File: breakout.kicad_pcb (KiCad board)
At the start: 2 copper layers, 50 x 50 mm, 98 parts

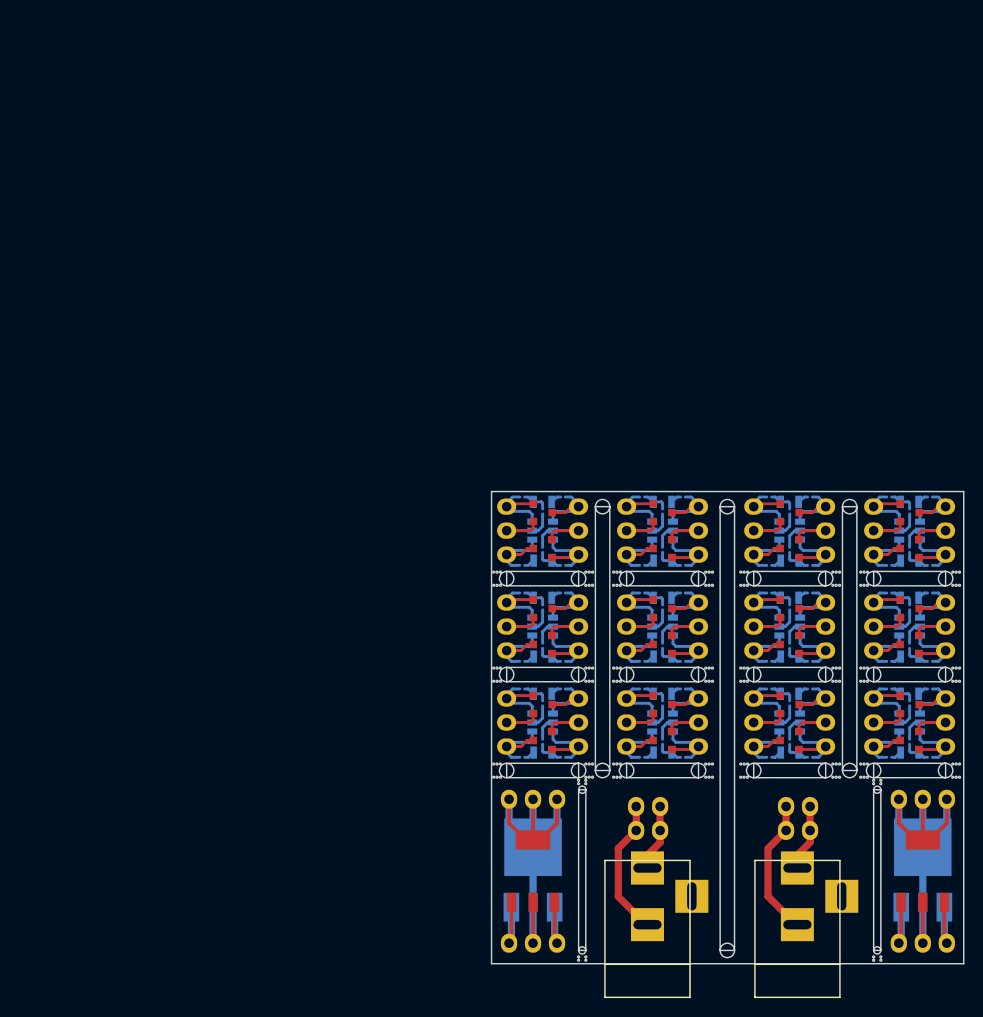
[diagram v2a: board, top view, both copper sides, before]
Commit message: 10x10 breakout with soic-8 and tssop-8
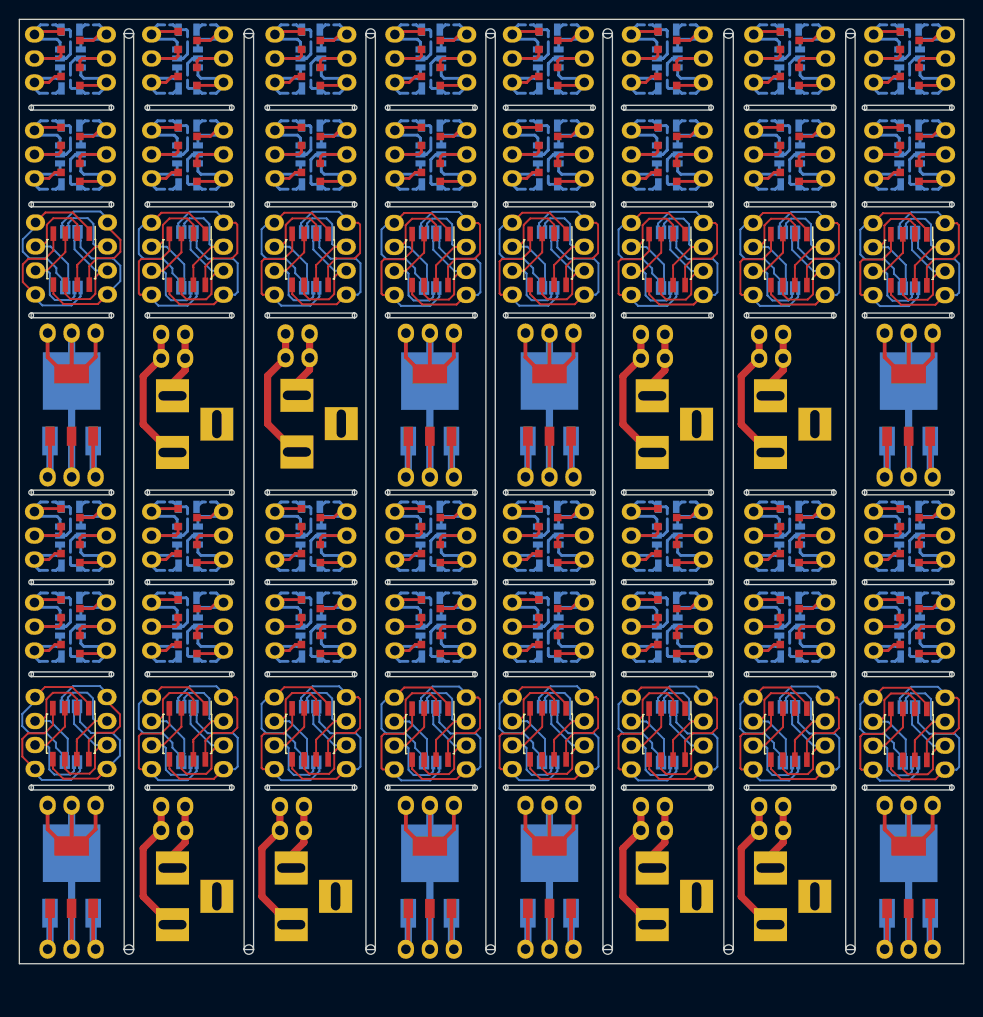
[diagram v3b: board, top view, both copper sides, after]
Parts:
- removed the REF** at (105.4, 124.5)
- removed the REF** at (105.4, 122.6)
- removed the REF** at (105.4, 126.4)
- removed the REF** at (101.6, 121.9)
- removed the REF** at (109.2, 121.9)
- removed the REF** at (105.4, 121.4)
- removed the REF** at (105.4, 127.6)
- removed the REF** at (118.1, 127.6)
- removed the REF** at (118.1, 121.4)
- removed the REF** at (121.9, 121.9)
- removed the REF** at (114.3, 121.9)
- removed the REF** at (118.1, 126.4)
- removed the REF** at (118.1, 122.6)
- removed the REF** at (118.1, 124.5)
- removed the REF** at (131.6, 124.5)
- removed the REF** at (131.6, 122.6)
- removed the REF** at (131.6, 126.4)
- removed the REF** at (127.8, 121.9)
- removed the REF** at (135.4, 121.9)
- removed the REF** at (131.6, 121.4)
- removed the REF** at (131.6, 127.6)
- removed the REF** at (144.3, 127.6)
- removed the REF** at (144.3, 121.4)
- removed the REF** at (148.1, 121.9)
- removed the REF** at (140.5, 121.9)
- removed the REF** at (144.3, 126.4)
- removed the REF** at (144.3, 122.6)
- removed the REF** at (144.3, 124.5)
- added REF**: TSSOP-8_4.4x3mm_Pitch0.65mm, Housings_SSOP:TSSOP-8_4.4x3mm_Pitch0.65mm, B.Cu at (106.0, 75.5)
- added REF**: SOIC-8_3.9x4.9mm_Pitch1.27mm, Housings_SOIC:SOIC-8_3.9x4.9mm_Pitch1.27mm, F.Cu at (118.6, 75.4)
- added REF**: SOT-23-6, TO_SOT_Packages_SMD:SOT-23-6, B.Cu at (131.6, 114.3)
- added REF**: R_0805, Resistors_SMD:R_0805, B.Cu at (118.6, 111.3)
- added REF**: R_0805, Resistors_SMD:R_0805, B.Cu at (118.6, 107.8)
- added REF**: R_0805, Resistors_SMD:R_0805, B.Cu at (106.0, 101.6)
- added REF**: SOT-23-6, TO_SOT_Packages_SMD:SOT-23-6, B.Cu at (118.6, 104.7)
- added REF**: R_0805, Resistors_SMD:R_0805, B.Cu at (106.0, 111.3)
- added REF**: SOT-23-6, TO_SOT_Packages_SMD:SOT-23-6, B.Cu at (106.0, 104.7)
- added REF**: R_0805, Resistors_SMD:R_0805, B.Cu at (118.6, 101.6)
- added REF**: R_0805, Resistors_SMD:R_0805, B.Cu at (106.0, 107.8)
- added REF**: R_0805, Resistors_SMD:R_0805, B.Cu at (144.3, 111.3)
- added REF**: Pin_Header_Straight_1x03, Pin_Headers:Pin_Header_Straight_1x03, F.Cu at (114.8, 71.6)
- added REF**: SOT-23-6, TO_SOT_Packages_SMD:SOT-23-6, B.Cu at (144.3, 114.3)
- added REF**: R_0805, Resistors_SMD:R_0805, B.Cu at (144.3, 107.8)
- added REF**: R_0805, Resistors_SMD:R_0805, B.Cu at (144.3, 101.6)
- added REF**: SOT-23-6, TO_SOT_Packages_SMD:SOT-23-6, B.Cu at (144.3, 104.7)
- added REF**: R_0805, Resistors_SMD:R_0805, B.Cu at (106.0, 117.5)
- added REF**: SOT-23-6, TO_SOT_Packages_SMD:SOT-23-6, B.Cu at (106.0, 114.3)
- added REF**: R_0805, Resistors_SMD:R_0805, B.Cu at (118.6, 117.5)
- added REF**: SOT-23-6, TO_SOT_Packages_SMD:SOT-23-6, B.Cu at (118.6, 114.3)
- added REF**: TO-252-2Lead, TO_SOT_Packages_SMD:TO-252-2Lead, B.Cu at (106.1, 144.6)
- added REF**: R_0805, Resistors_SMD:R_0805, B.Cu at (93.6, 117.5)
- added REF**: Pin_Header_Straight_1x03, Pin_Headers:Pin_Header_Straight_1x03, F.Cu at (109.8, 71.5)
- added REF**: R_0805, Resistors_SMD:R_0805, B.Cu at (80.9, 117.5)
- added REF**: TO-252-2Lead, TO_SOT_Packages_SMD:TO-252-2Lead, B.Cu at (93.5, 144.7)
- added REF**: Pin_Header_Straight_1x03, Pin_Headers:Pin_Header_Straight_1x03, F.Cu at (109.8, 102.1)
- added REF**: Pin_Header_Straight_1x03, Pin_Headers:Pin_Header_Straight_1x03, F.Cu at (102.2, 102.1)
- added REF**: Pin_Header_Straight_1x03, Pin_Headers:Pin_Header_Straight_1x03, F.Cu at (114.8, 102.1)
- added REF**: SOT-23, TO_SOT_Packages_SMD:SOT-23, F.Cu at (106.0, 106.6)
- added REF**: SOT-23, TO_SOT_Packages_SMD:SOT-23, F.Cu at (106.0, 102.8)
- added REF**: Pin_Header_Straight_1x03, Pin_Headers:Pin_Header_Straight_1x03, F.Cu at (114.8, 111.8)
- added REF**: Pin_Header_Straight_1x03, Pin_Headers:Pin_Header_Straight_1x03, F.Cu at (109.8, 111.8)
- added REF**: SOT-23, TO_SOT_Packages_SMD:SOT-23, F.Cu at (106.0, 112.4)
- added REF**: SOIC-8_3.9x4.9mm_Pitch1.27mm, Housings_SOIC:SOIC-8_3.9x4.9mm_Pitch1.27mm, F.Cu at (106.0, 75.4)
- added REF**: Pin_Header_Straight_1x03, Pin_Headers:Pin_Header_Straight_1x03, F.Cu at (102.2, 111.8)
- added REF**: SOT-23, TO_SOT_Packages_SMD:SOT-23, F.Cu at (106.0, 116.2)
- added REF**: Pin_Header_Straight_1x03, Pin_Headers:Pin_Header_Straight_1x03, F.Cu at (141.6, 148.5)
- added REF**: Pin_Header_Straight_1x03, Pin_Headers:Pin_Header_Straight_1x03, F.Cu at (128.3, 135.9)
- added REF**: SOT-223, TO_SOT_Packages_SMD:SOT-223, F.Cu at (144.2, 140.8)
- added REF**: Pin_Header_Straight_1x03, Pin_Headers:Pin_Header_Straight_1x03, F.Cu at (141.6, 133.2)
- added REF**: Pin_Header_Straight_1x03, Pin_Headers:Pin_Header_Straight_1x03, F.Cu at (128.3, 133.3)
- added REF**: Pin_Header_Straight_1x03, Pin_Headers:Pin_Header_Straight_1x03, F.Cu at (103.6, 148.5)
- added REF**: SOT-223, TO_SOT_Packages_SMD:SOT-223, F.Cu at (106.1, 140.8)
- added REF**: Pin_Header_Straight_1x03, Pin_Headers:Pin_Header_Straight_1x03, F.Cu at (103.6, 133.2)
- added REF**: Pin_Header_Straight_1x03, Pin_Headers:Pin_Header_Straight_1x03, F.Cu at (122.4, 71.6)
- added REF**: Pin_Header_Straight_1x03, Pin_Headers:Pin_Header_Straight_1x03, F.Cu at (115.8, 133.3)
- added REF**: Pin_Header_Straight_1x03, Pin_Headers:Pin_Header_Straight_1x03, F.Cu at (115.8, 135.9)
- added REF**: Pin_Header_Straight_1x03, Pin_Headers:Pin_Header_Straight_1x03, F.Cu at (77.6, 135.9)
- added REF**: Pin_Header_Straight_1x03, Pin_Headers:Pin_Header_Straight_1x03, F.Cu at (77.6, 133.3)
- added REF**: SOT-23, TO_SOT_Packages_SMD:SOT-23, F.Cu at (93.6, 106.6)
- added REF**: Pin_Header_Straight_1x03, Pin_Headers:Pin_Header_Straight_1x03, F.Cu at (89.8, 102.1)
- added REF**: SOT-23, TO_SOT_Packages_SMD:SOT-23, F.Cu at (93.6, 102.8)
- added REF**: Pin_Header_Straight_1x03, Pin_Headers:Pin_Header_Straight_1x03, F.Cu at (97.4, 102.1)
- added REF**: Pin_Header_Straight_1x03, Pin_Headers:Pin_Header_Straight_1x03, F.Cu at (77.1, 111.8)
- added REF**: SOT-23, TO_SOT_Packages_SMD:SOT-23, F.Cu at (80.9, 112.4)
- added REF**: Pin_Header_Straight_1x03, Pin_Headers:Pin_Header_Straight_1x03, F.Cu at (84.6, 71.5)
- added REF**: Pin_Header_Straight_1x03, Pin_Headers:Pin_Header_Straight_1x03, F.Cu at (77.1, 102.1)
- added REF**: SOT-23, TO_SOT_Packages_SMD:SOT-23, F.Cu at (80.9, 106.6)
- added REF**: SOT-23, TO_SOT_Packages_SMD:SOT-23, F.Cu at (80.9, 116.2)
- added REF**: Pin_Header_Straight_1x03, Pin_Headers:Pin_Header_Straight_1x03, F.Cu at (84.7, 102.1)
- added REF**: SOT-23, TO_SOT_Packages_SMD:SOT-23, F.Cu at (80.9, 102.8)
- added REF**: SOT-23, TO_SOT_Packages_SMD:SOT-23, F.Cu at (93.6, 116.2)
- added REF**: Pin_Header_Straight_1x03, Pin_Headers:Pin_Header_Straight_1x03, F.Cu at (89.8, 111.8)
- added REF**: Pin_Header_Straight_1x03, Pin_Headers:Pin_Header_Straight_1x03, F.Cu at (97.4, 111.8)
- added REF**: Pin_Header_Straight_1x03, Pin_Headers:Pin_Header_Straight_1x03, F.Cu at (84.7, 111.8)
- added REF**: SOT-23, TO_SOT_Packages_SMD:SOT-23, F.Cu at (93.6, 112.4)
- added REF**: SOIC-8_3.9x4.9mm_Pitch1.27mm, Housings_SOIC:SOIC-8_3.9x4.9mm_Pitch1.27mm, F.Cu at (80.8, 75.4)
- added REF**: Pin_Header_Straight_1x03, Pin_Headers:Pin_Header_Straight_1x03, F.Cu at (90.9, 133.2)
- added REF**: SOT-223, TO_SOT_Packages_SMD:SOT-223, F.Cu at (93.5, 140.8)
- added REF**: Pin_Header_Straight_1x03, Pin_Headers:Pin_Header_Straight_1x03, F.Cu at (90.9, 148.5)
- added REF**: Pin_Header_Straight_1x03, Pin_Headers:Pin_Header_Straight_1x03, F.Cu at (71.6, 102.1)
- added REF**: Pin_Header_Straight_1x03, Pin_Headers:Pin_Header_Straight_1x03, F.Cu at (64.0, 102.1)
- added REF**: SOT-23, TO_SOT_Packages_SMD:SOT-23, F.Cu at (67.8, 102.8)
- added REF**: SOT-23, TO_SOT_Packages_SMD:SOT-23, F.Cu at (67.8, 106.6)
- added REF**: Pin_Header_Straight_1x03, Pin_Headers:Pin_Header_Straight_1x03, F.Cu at (65.0, 133.3)
- added REF**: Pin_Header_Straight_1x03, Pin_Headers:Pin_Header_Straight_1x03, F.Cu at (53.0, 148.5)
- added REF**: SOT-223, TO_SOT_Packages_SMD:SOT-223, F.Cu at (55.5, 140.8)
- added REF**: Pin_Header_Straight_1x03, Pin_Headers:Pin_Header_Straight_1x03, F.Cu at (89.7, 71.6)
- added REF**: Pin_Header_Straight_1x03, Pin_Headers:Pin_Header_Straight_1x03, F.Cu at (65.0, 135.9)
- added REF**: Pin_Header_Straight_1x03, Pin_Headers:Pin_Header_Straight_1x03, F.Cu at (53.0, 133.2)
- added REF**: Pin_Header_Straight_1x03, Pin_Headers:Pin_Header_Straight_1x03, F.Cu at (51.6, 102.1)
- added REF**: Pin_Header_Straight_1x03, Pin_Headers:Pin_Header_Straight_1x03, F.Cu at (59.2, 102.1)
- added REF**: SOT-23, TO_SOT_Packages_SMD:SOT-23, F.Cu at (55.4, 106.6)
- added REF**: SOT-23, TO_SOT_Packages_SMD:SOT-23, F.Cu at (55.4, 102.8)
- added REF**: SOIC-8_3.9x4.9mm_Pitch1.27mm, Housings_SOIC:SOIC-8_3.9x4.9mm_Pitch1.27mm, F.Cu at (55.5, 125.6)
- added REF**: Pin_Header_Straight_1x03, Pin_Headers:Pin_Header_Straight_1x03, F.Cu at (59.3, 121.8)
- added REF**: Pin_Header_Straight_1x03, Pin_Headers:Pin_Header_Straight_1x03, F.Cu at (51.7, 121.8)
- added REF**: SOT-23, TO_SOT_Packages_SMD:SOT-23, F.Cu at (67.8, 116.2)
- added REF**: SOIC-8_3.9x4.9mm_Pitch1.27mm, Housings_SOIC:SOIC-8_3.9x4.9mm_Pitch1.27mm, F.Cu at (93.5, 75.4)
- added REF**: SOT-23, TO_SOT_Packages_SMD:SOT-23, F.Cu at (67.8, 112.4)
- added REF**: Pin_Header_Straight_1x03, Pin_Headers:Pin_Header_Straight_1x03, F.Cu at (64.0, 111.8)
- added REF**: Pin_Header_Straight_1x03, Pin_Headers:Pin_Header_Straight_1x03, F.Cu at (71.6, 111.8)
- added REF**: SOT-23, TO_SOT_Packages_SMD:SOT-23, F.Cu at (55.4, 112.4)
- added REF**: SOT-23, TO_SOT_Packages_SMD:SOT-23, F.Cu at (55.4, 116.2)
- added REF**: Pin_Header_Straight_1x03, Pin_Headers:Pin_Header_Straight_1x03, F.Cu at (51.6, 111.8)
- added REF**: Pin_Header_Straight_1x03, Pin_Headers:Pin_Header_Straight_1x03, F.Cu at (59.2, 111.8)
- added REF**: Pin_Header_Straight_1x03, Pin_Headers:Pin_Header_Straight_1x03, F.Cu at (122.4, 102.1)
- added REF**: SOT-23, TO_SOT_Packages_SMD:SOT-23, F.Cu at (118.6, 102.8)
- added REF**: SOT-23, TO_SOT_Packages_SMD:SOT-23, F.Cu at (118.6, 106.6)
- added REF**: Pin_Header_Straight_1x03, Pin_Headers:Pin_Header_Straight_1x03, F.Cu at (97.3, 71.6)
- added REF**: Pin_Header_Straight_1x03, Pin_Headers:Pin_Header_Straight_1x03, F.Cu at (127.8, 102.1)
- added REF**: Pin_Header_Straight_1x03, Pin_Headers:Pin_Header_Straight_1x03, F.Cu at (127.8, 111.8)
- added REF**: SOT-23, TO_SOT_Packages_SMD:SOT-23, F.Cu at (131.6, 116.2)
- added REF**: SOT-23, TO_SOT_Packages_SMD:SOT-23, F.Cu at (118.6, 112.4)
- added REF**: SOT-23, TO_SOT_Packages_SMD:SOT-23, F.Cu at (131.6, 112.4)
- added REF**: Pin_Header_Straight_1x03, Pin_Headers:Pin_Header_Straight_1x03, F.Cu at (122.4, 111.8)
- added REF**: SOT-23, TO_SOT_Packages_SMD:SOT-23, F.Cu at (118.6, 116.2)
- added REF**: SOT-23, TO_SOT_Packages_SMD:SOT-23, F.Cu at (131.6, 102.8)
- added REF**: SOT-23, TO_SOT_Packages_SMD:SOT-23, F.Cu at (144.3, 102.8)
- added REF**: SOT-23, TO_SOT_Packages_SMD:SOT-23, F.Cu at (144.3, 106.6)
- added REF**: TSSOP-8_4.4x3mm_Pitch0.65mm, Housings_SSOP:TSSOP-8_4.4x3mm_Pitch0.65mm, B.Cu at (118.6, 75.5)
- added REF**: SOIC-8_3.9x4.9mm_Pitch1.27mm, Housings_SOIC:SOIC-8_3.9x4.9mm_Pitch1.27mm, F.Cu at (55.5, 75.4)
- added REF**: Pin_Header_Straight_1x03, Pin_Headers:Pin_Header_Straight_1x03, F.Cu at (135.4, 102.1)
- added REF**: Pin_Header_Straight_1x03, Pin_Headers:Pin_Header_Straight_1x03, F.Cu at (140.5, 102.1)
- added REF**: Pin_Header_Straight_1x03, Pin_Headers:Pin_Header_Straight_1x03, F.Cu at (148.1, 102.1)
- added REF**: SOT-23, TO_SOT_Packages_SMD:SOT-23, F.Cu at (131.6, 106.6)
- added REF**: Pin_Header_Straight_1x03, Pin_Headers:Pin_Header_Straight_1x03, F.Cu at (140.5, 111.8)
- added REF**: Pin_Header_Straight_1x03, Pin_Headers:Pin_Header_Straight_1x03, F.Cu at (148.1, 111.8)
- added REF**: SOT-23, TO_SOT_Packages_SMD:SOT-23, F.Cu at (144.3, 116.2)
- added REF**: Pin_Header_Straight_1x03, Pin_Headers:Pin_Header_Straight_1x03, F.Cu at (135.4, 111.8)
- added REF**: SOT-23, TO_SOT_Packages_SMD:SOT-23, F.Cu at (144.3, 112.4)
- added REF**: TO-252-2Lead, TO_SOT_Packages_SMD:TO-252-2Lead, B.Cu at (144.2, 94.7)
- added REF**: Pin_Header_Straight_1x03, Pin_Headers:Pin_Header_Straight_1x03, F.Cu at (71.6, 71.5)
- added REF**: R_0805, Resistors_SMD:R_0805, B.Cu at (144.3, 67.5)
- added REF**: SOT-23-6, TO_SOT_Packages_SMD:SOT-23-6, B.Cu at (106.0, 54.1)
- added REF**: R_0805, Resistors_SMD:R_0805, B.Cu at (106.0, 57.3)
- added REF**: R_0805, Resistors_SMD:R_0805, B.Cu at (118.6, 51.1)
- added REF**: R_0805, Resistors_SMD:R_0805, B.Cu at (106.0, 51.1)
- added REF**: R_0805, Resistors_SMD:R_0805, B.Cu at (144.3, 61.3)
- added REF**: R_0805, Resistors_SMD:R_0805, B.Cu at (144.3, 57.3)
- added REF**: R_0805, Resistors_SMD:R_0805, B.Cu at (144.3, 51.1)
- added REF**: SOT-23-6, TO_SOT_Packages_SMD:SOT-23-6, B.Cu at (144.3, 54.1)
- added REF**: SOT-23-6, TO_SOT_Packages_SMD:SOT-23-6, B.Cu at (144.3, 64.3)
- added REF**: Pin_Header_Straight_1x03, Pin_Headers:Pin_Header_Straight_1x03, F.Cu at (77.0, 71.5)
- added REF**: R_0805, Resistors_SMD:R_0805, B.Cu at (106.0, 67.5)
- added REF**: TO-252-2Lead, TO_SOT_Packages_SMD:TO-252-2Lead, B.Cu at (106.1, 94.6)
- added REF**: SOT-23-6, TO_SOT_Packages_SMD:SOT-23-6, B.Cu at (106.0, 64.3)
- added REF**: R_0805, Resistors_SMD:R_0805, B.Cu at (106.0, 61.3)
- added REF**: R_0805, Resistors_SMD:R_0805, B.Cu at (118.6, 57.3)
- added REF**: R_0805, Resistors_SMD:R_0805, B.Cu at (118.6, 67.5)
- added REF**: SOT-23-6, TO_SOT_Packages_SMD:SOT-23-6, B.Cu at (118.6, 54.1)
- added REF**: SOT-23-6, TO_SOT_Packages_SMD:SOT-23-6, B.Cu at (118.6, 64.3)
- added REF**: R_0805, Resistors_SMD:R_0805, B.Cu at (118.6, 61.3)
- added REF**: SOT-23-6, TO_SOT_Packages_SMD:SOT-23-6, B.Cu at (131.6, 54.1)
- added REF**: SOIC-8_3.9x4.9mm_Pitch1.27mm, Housings_SOIC:SOIC-8_3.9x4.9mm_Pitch1.27mm, F.Cu at (67.8, 75.4)
- added REF**: R_0805, Resistors_SMD:R_0805, B.Cu at (131.6, 57.3)
- added REF**: SOT-23-6, TO_SOT_Packages_SMD:SOT-23-6, B.Cu at (131.6, 64.3)
- added REF**: R_0805, Resistors_SMD:R_0805, B.Cu at (131.6, 67.5)
- added REF**: R_0805, Resistors_SMD:R_0805, B.Cu at (131.6, 61.3)
- added REF**: R_0805, Resistors_SMD:R_0805, B.Cu at (131.6, 51.1)
- added REF**: Pin_Header_Straight_1x03, Pin_Headers:Pin_Header_Straight_1x03, F.Cu at (109.8, 61.8)
- added REF**: Pin_Header_Straight_1x03, Pin_Headers:Pin_Header_Straight_1x03, F.Cu at (102.2, 61.8)
- added REF**: SOT-23, TO_SOT_Packages_SMD:SOT-23, F.Cu at (118.6, 62.4)
- added REF**: SOT-23, TO_SOT_Packages_SMD:SOT-23, F.Cu at (118.6, 66.2)
- added REF**: Pin_Header_Straight_1x03, Pin_Headers:Pin_Header_Straight_1x03, F.Cu at (114.8, 61.8)
- added REF**: Pin_Header_Straight_1x03, Pin_Headers:Pin_Header_Straight_1x03, F.Cu at (64.0, 71.5)
- added REF**: Pin_Header_Straight_1x03, Pin_Headers:Pin_Header_Straight_1x03, F.Cu at (122.4, 61.8)
- added REF**: SOT-23, TO_SOT_Packages_SMD:SOT-23, F.Cu at (106.0, 52.2)
- added REF**: SOT-23, TO_SOT_Packages_SMD:SOT-23, F.Cu at (106.0, 62.4)
- added REF**: Pin_Header_Straight_1x03, Pin_Headers:Pin_Header_Straight_1x03, F.Cu at (102.2, 51.6)
- added REF**: Pin_Header_Straight_1x03, Pin_Headers:Pin_Header_Straight_1x03, F.Cu at (109.8, 51.6)
- added REF**: SOT-23, TO_SOT_Packages_SMD:SOT-23, F.Cu at (106.0, 66.2)
- added REF**: SOT-23, TO_SOT_Packages_SMD:SOT-23, F.Cu at (106.0, 56.0)
- added REF**: Pin_Header_Straight_1x03, Pin_Headers:Pin_Header_Straight_1x03, F.Cu at (114.8, 51.6)
- added REF**: SOT-23, TO_SOT_Packages_SMD:SOT-23, F.Cu at (118.6, 56.0)
- added REF**: SOT-23, TO_SOT_Packages_SMD:SOT-23, F.Cu at (118.6, 52.2)
- added REF**: Pin_Header_Straight_1x03, Pin_Headers:Pin_Header_Straight_1x03, F.Cu at (59.3, 71.5)
- added REF**: SOT-23, TO_SOT_Packages_SMD:SOT-23, F.Cu at (131.6, 52.2)
- added REF**: SOT-23, TO_SOT_Packages_SMD:SOT-23, F.Cu at (131.6, 56.0)
- added REF**: Pin_Header_Straight_1x03, Pin_Headers:Pin_Header_Straight_1x03, F.Cu at (127.8, 51.6)
- added REF**: Pin_Header_Straight_1x03, Pin_Headers:Pin_Header_Straight_1x03, F.Cu at (122.4, 51.6)
- added REF**: Pin_Header_Straight_1x03, Pin_Headers:Pin_Header_Straight_1x03, F.Cu at (135.4, 51.6)
- added REF**: Pin_Header_Straight_1x03, Pin_Headers:Pin_Header_Straight_1x03, F.Cu at (148.1, 61.8)
- added REF**: Pin_Header_Straight_1x03, Pin_Headers:Pin_Header_Straight_1x03, F.Cu at (148.1, 51.6)
- added REF**: Pin_Header_Straight_1x03, Pin_Headers:Pin_Header_Straight_1x03, F.Cu at (140.5, 51.6)
- added REF**: SOT-23, TO_SOT_Packages_SMD:SOT-23, F.Cu at (144.3, 56.0)
- added REF**: SOT-23, TO_SOT_Packages_SMD:SOT-23, F.Cu at (144.3, 52.2)
- added REF**: Pin_Header_Straight_1x03, Pin_Headers:Pin_Header_Straight_1x03, F.Cu at (51.7, 71.5)
- added REF**: SOT-23, TO_SOT_Packages_SMD:SOT-23, F.Cu at (144.3, 62.4)
- added REF**: SOT-23, TO_SOT_Packages_SMD:SOT-23, F.Cu at (144.3, 66.2)
- added REF**: Pin_Header_Straight_1x03, Pin_Headers:Pin_Header_Straight_1x03, F.Cu at (140.5, 61.8)
- added REF**: SOT-23, TO_SOT_Packages_SMD:SOT-23, F.Cu at (131.6, 66.2)
- added REF**: Pin_Header_Straight_1x03, Pin_Headers:Pin_Header_Straight_1x03, F.Cu at (135.4, 61.8)
- added REF**: Pin_Header_Straight_1x03, Pin_Headers:Pin_Header_Straight_1x03, F.Cu at (127.8, 61.8)
- added REF**: SOT-23, TO_SOT_Packages_SMD:SOT-23, F.Cu at (131.6, 62.4)
- added REF**: Pin_Header_Straight_1x03, Pin_Headers:Pin_Header_Straight_1x03, F.Cu at (128.3, 83.3)
- added REF**: Pin_Header_Straight_1x03, Pin_Headers:Pin_Header_Straight_1x03, F.Cu at (128.3, 85.9)
- added REF**: Pin_Header_Straight_1x03, Pin_Headers:Pin_Header_Straight_1x03, F.Cu at (141.6, 83.2)
- added REF**: Pin_Header_Straight_1x03, Pin_Headers:Pin_Header_Straight_1x03, F.Cu at (148.0, 71.6)
- added REF**: Pin_Header_Straight_1x03, Pin_Headers:Pin_Header_Straight_1x03, F.Cu at (141.6, 98.5)
- added REF**: SOT-223, TO_SOT_Packages_SMD:SOT-223, F.Cu at (144.2, 90.8)
- added REF**: Pin_Header_Straight_1x03, Pin_Headers:Pin_Header_Straight_1x03, F.Cu at (115.8, 85.9)
- added REF**: Pin_Header_Straight_1x03, Pin_Headers:Pin_Header_Straight_1x03, F.Cu at (103.6, 83.2)
- added REF**: Pin_Header_Straight_1x03, Pin_Headers:Pin_Header_Straight_1x03, F.Cu at (115.8, 83.3)
- added REF**: Pin_Header_Straight_1x03, Pin_Headers:Pin_Header_Straight_1x03, F.Cu at (103.6, 98.5)
- added REF**: SOT-223, TO_SOT_Packages_SMD:SOT-223, F.Cu at (106.1, 90.8)
- added REF**: Pin_Header_Straight_1x03, Pin_Headers:Pin_Header_Straight_1x03, F.Cu at (140.4, 71.6)
- added REF**: Pin_Header_Straight_1x03, Pin_Headers:Pin_Header_Straight_1x03, F.Cu at (135.3, 71.6)
- added REF**: TSSOP-8_4.4x3mm_Pitch0.65mm, Housings_SSOP:TSSOP-8_4.4x3mm_Pitch0.65mm, B.Cu at (131.5, 75.5)
- added REF**: SOIC-8_3.9x4.9mm_Pitch1.27mm, Housings_SOIC:SOIC-8_3.9x4.9mm_Pitch1.27mm, F.Cu at (131.5, 75.4)
- added REF**: SOIC-8_3.9x4.9mm_Pitch1.27mm, Housings_SOIC:SOIC-8_3.9x4.9mm_Pitch1.27mm, F.Cu at (144.2, 75.5)
- added REF**: Pin_Header_Straight_1x03, Pin_Headers:Pin_Header_Straight_1x03, F.Cu at (127.7, 71.6)
- added REF**: TSSOP-8_4.4x3mm_Pitch0.65mm, Housings_SSOP:TSSOP-8_4.4x3mm_Pitch0.65mm, B.Cu at (144.2, 125.8)
- added REF**: TSSOP-8_4.4x3mm_Pitch0.65mm, Housings_SSOP:TSSOP-8_4.4x3mm_Pitch0.65mm, B.Cu at (131.5, 125.8)
- added REF**: TSSOP-8_4.4x3mm_Pitch0.65mm, Housings_SSOP:TSSOP-8_4.4x3mm_Pitch0.65mm, B.Cu at (106.0, 125.7)
- added REF**: TSSOP-8_4.4x3mm_Pitch0.65mm, Housings_SSOP:TSSOP-8_4.4x3mm_Pitch0.65mm, B.Cu at (118.6, 125.8)
- added REF**: SOIC-8_3.9x4.9mm_Pitch1.27mm, Housings_SOIC:SOIC-8_3.9x4.9mm_Pitch1.27mm, F.Cu at (144.2, 125.7)
- added REF**: Pin_Header_Straight_1x03, Pin_Headers:Pin_Header_Straight_1x03, F.Cu at (135.3, 121.8)
- added REF**: SOIC-8_3.9x4.9mm_Pitch1.27mm, Housings_SOIC:SOIC-8_3.9x4.9mm_Pitch1.27mm, F.Cu at (131.5, 125.7)
- added REF**: TSSOP-8_4.4x3mm_Pitch0.65mm, Housings_SSOP:TSSOP-8_4.4x3mm_Pitch0.65mm, B.Cu at (144.2, 75.5)
- added REF**: Pin_Header_Straight_1x03, Pin_Headers:Pin_Header_Straight_1x03, F.Cu at (148.0, 121.8)
- added REF**: Pin_Header_Straight_1x03, Pin_Headers:Pin_Header_Straight_1x03, F.Cu at (140.4, 121.8)
- added REF**: Pin_Header_Straight_1x03, Pin_Headers:Pin_Header_Straight_1x03, F.Cu at (127.7, 121.8)
- added REF**: Pin_Header_Straight_1x03, Pin_Headers:Pin_Header_Straight_1x03, F.Cu at (122.4, 121.8)
- added REF**: Pin_Header_Straight_1x03, Pin_Headers:Pin_Header_Straight_1x03, F.Cu at (114.8, 121.8)
- added REF**: SOIC-8_3.9x4.9mm_Pitch1.27mm, Housings_SOIC:SOIC-8_3.9x4.9mm_Pitch1.27mm, F.Cu at (118.6, 125.7)
- added REF**: Pin_Header_Straight_1x03, Pin_Headers:Pin_Header_Straight_1x03, F.Cu at (109.8, 121.8)
- added REF**: SOIC-8_3.9x4.9mm_Pitch1.27mm, Housings_SOIC:SOIC-8_3.9x4.9mm_Pitch1.27mm, F.Cu at (106.0, 125.7)
- added REF**: Pin_Header_Straight_1x03, Pin_Headers:Pin_Header_Straight_1x03, F.Cu at (102.2, 121.8)
- added REF**: TSSOP-8_4.4x3mm_Pitch0.65mm, Housings_SSOP:TSSOP-8_4.4x3mm_Pitch0.65mm, B.Cu at (93.5, 125.8)
- added REF**: TSSOP-8_4.4x3mm_Pitch0.65mm, Housings_SSOP:TSSOP-8_4.4x3mm_Pitch0.65mm, B.Cu at (80.8, 75.5)
- added REF**: TSSOP-8_4.4x3mm_Pitch0.65mm, Housings_SSOP:TSSOP-8_4.4x3mm_Pitch0.65mm, B.Cu at (80.8, 125.7)
- added REF**: Pin_Header_Straight_1x03, Pin_Headers:Pin_Header_Straight_1x03, F.Cu at (97.3, 121.8)
- added REF**: Pin_Header_Straight_1x03, Pin_Headers:Pin_Header_Straight_1x03, F.Cu at (77.0, 121.8)
- added REF**: SOIC-8_3.9x4.9mm_Pitch1.27mm, Housings_SOIC:SOIC-8_3.9x4.9mm_Pitch1.27mm, F.Cu at (80.8, 125.7)
- added REF**: SOIC-8_3.9x4.9mm_Pitch1.27mm, Housings_SOIC:SOIC-8_3.9x4.9mm_Pitch1.27mm, F.Cu at (93.5, 125.7)
- added REF**: Pin_Header_Straight_1x03, Pin_Headers:Pin_Header_Straight_1x03, F.Cu at (89.7, 121.8)
- added REF**: Pin_Header_Straight_1x03, Pin_Headers:Pin_Header_Straight_1x03, F.Cu at (84.6, 121.8)
- added REF**: TSSOP-8_4.4x3mm_Pitch0.65mm, Housings_SSOP:TSSOP-8_4.4x3mm_Pitch0.65mm, B.Cu at (67.8, 125.7)
- added REF**: Pin_Header_Straight_1x03, Pin_Headers:Pin_Header_Straight_1x03, F.Cu at (71.6, 121.8)
- added REF**: Pin_Header_Straight_1x03, Pin_Headers:Pin_Header_Straight_1x03, F.Cu at (64.0, 121.8)
- added REF**: TSSOP-8_4.4x3mm_Pitch0.65mm, Housings_SSOP:TSSOP-8_4.4x3mm_Pitch0.65mm, B.Cu at (93.5, 75.5)
- added REF**: SOIC-8_3.9x4.9mm_Pitch1.27mm, Housings_SOIC:SOIC-8_3.9x4.9mm_Pitch1.27mm, F.Cu at (67.8, 125.7)
- added REF**: BARREL_JACK, Connect:BARREL_JACK, F.Cu at (129.5, 146.1)
- added REF**: BARREL_JACK, Connect:BARREL_JACK, F.Cu at (117.0, 146.1)
- added REF**: BARREL_JACK, Connect:BARREL_JACK, F.Cu at (78.8, 146.1)
- added REF**: BARREL_JACK, Connect:BARREL_JACK, F.Cu at (66.2, 146.1)
- added REF**: BARREL_JACK, Connect:BARREL_JACK, F.Cu at (129.5, 96.1)
- added REF**: BARREL_JACK, Connect:BARREL_JACK, F.Cu at (117.0, 96.1)
- added REF**: R_0805, Resistors_SMD:R_0805, B.Cu at (67.8, 107.8)
- added REF**: TSSOP-8_4.4x3mm_Pitch0.65mm, Housings_SSOP:TSSOP-8_4.4x3mm_Pitch0.65mm, B.Cu at (55.5, 75.5)
- added REF**: R_0805, Resistors_SMD:R_0805, B.Cu at (67.8, 101.6)
- added REF**: SOT-23-6, TO_SOT_Packages_SMD:SOT-23-6, B.Cu at (55.4, 104.7)
- added REF**: SOT-23-6, TO_SOT_Packages_SMD:SOT-23-6, B.Cu at (67.8, 104.7)
- added REF**: R_0805, Resistors_SMD:R_0805, B.Cu at (55.4, 101.6)
- added REF**: R_0805, Resistors_SMD:R_0805, B.Cu at (55.4, 107.8)
- added REF**: TSSOP-8_4.4x3mm_Pitch0.65mm, Housings_SSOP:TSSOP-8_4.4x3mm_Pitch0.65mm, B.Cu at (55.5, 125.7)
- added REF**: R_0805, Resistors_SMD:R_0805, B.Cu at (55.4, 111.3)
- added REF**: SOT-23-6, TO_SOT_Packages_SMD:SOT-23-6, B.Cu at (55.4, 114.3)
- added REF**: TO-252-2Lead, TO_SOT_Packages_SMD:TO-252-2Lead, B.Cu at (55.5, 144.6)
- added REF**: R_0805, Resistors_SMD:R_0805, B.Cu at (55.4, 117.5)
- added REF**: TSSOP-8_4.4x3mm_Pitch0.65mm, Housings_SSOP:TSSOP-8_4.4x3mm_Pitch0.65mm, B.Cu at (67.8, 75.5)
- added REF**: SOT-23-6, TO_SOT_Packages_SMD:SOT-23-6, B.Cu at (67.8, 114.3)
- added REF**: R_0805, Resistors_SMD:R_0805, B.Cu at (67.8, 117.5)
- added REF**: R_0805, Resistors_SMD:R_0805, B.Cu at (67.8, 111.3)
- added REF**: R_0805, Resistors_SMD:R_0805, B.Cu at (93.6, 101.6)
- added REF**: R_0805, Resistors_SMD:R_0805, B.Cu at (93.6, 107.8)
- added REF**: SOT-23-6, TO_SOT_Packages_SMD:SOT-23-6, B.Cu at (93.6, 114.3)
- added REF**: SOT-23-6, TO_SOT_Packages_SMD:SOT-23-6, B.Cu at (93.6, 104.7)
- added REF**: R_0805, Resistors_SMD:R_0805, B.Cu at (93.6, 111.3)
- added REF**: R_0805, Resistors_SMD:R_0805, B.Cu at (80.9, 107.8)
- added REF**: R_0805, Resistors_SMD:R_0805, B.Cu at (80.9, 101.6)
- added REF**: Pin_Header_Straight_1x03, Pin_Headers:Pin_Header_Straight_1x03, F.Cu at (102.2, 71.5)
- added REF**: R_0805, Resistors_SMD:R_0805, B.Cu at (80.9, 111.3)
- added REF**: SOT-23-6, TO_SOT_Packages_SMD:SOT-23-6, B.Cu at (80.9, 114.3)
- added REF**: SOT-23-6, TO_SOT_Packages_SMD:SOT-23-6, B.Cu at (80.9, 104.7)
- added REF**: TO-252-2Lead, TO_SOT_Packages_SMD:TO-252-2Lead, B.Cu at (144.2, 144.7)
- added REF**: R_0805, Resistors_SMD:R_0805, B.Cu at (144.3, 117.5)
- added REF**: R_0805, Resistors_SMD:R_0805, B.Cu at (131.6, 101.6)
- added REF**: R_0805, Resistors_SMD:R_0805, B.Cu at (131.6, 117.5)
- added REF**: SOT-23-6, TO_SOT_Packages_SMD:SOT-23-6, B.Cu at (131.6, 104.7)
- added REF**: R_0805, Resistors_SMD:R_0805, B.Cu at (131.6, 107.8)
- added REF**: R_0805, Resistors_SMD:R_0805, B.Cu at (131.6, 111.3)
- moved REF** 72.9 mm to (78.2, 85.8)
- moved REF** 72.9 mm to (78.2, 83.3)
- moved REF** 72.9 mm to (79.4, 96.0)
- moved REF** 71.8 mm to (93.5, 94.7)
- moved REF** 71.8 mm to (93.5, 90.8)
- moved REF** 71.8 mm to (90.9, 98.5)
- moved REF** 71.8 mm to (90.9, 83.2)
- moved REF** 71.2 mm to (80.9, 64.3)
- moved REF** 71.2 mm to (80.9, 66.2)
- moved REF** 71.2 mm to (77.1, 61.8)
- moved REF** 71.2 mm to (84.7, 61.8)
- moved REF** 71.2 mm to (80.9, 67.5)
- moved REF** 71.2 mm to (80.9, 57.3)
- moved REF** 71.2 mm to (80.9, 51.1)
- moved REF** 71.2 mm to (80.9, 56.0)
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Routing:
- net (no net): track 941.3 -> 4772.5 mm
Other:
- board size 50 x 50 mm -> 100 x 100 mm
